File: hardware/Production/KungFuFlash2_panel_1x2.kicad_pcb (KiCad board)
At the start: 2 copper layers, 140.3 x 70 mm, 114 parts, among them J1 DNP, J2 USB_C_Receptacle_USB2.0, J3 DNP, Q1 BC817-40, SW1 ES411X-10XX-43X-16-B, SW2 ES411X-10XX-43X-16-B, SW3 ES411X-10XX-43X-16-B, U1 Edge Connector, Immersion gol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, U2 AMS1117-3.3, U3 STM32H7B0VBTx, Y1 25 MHz

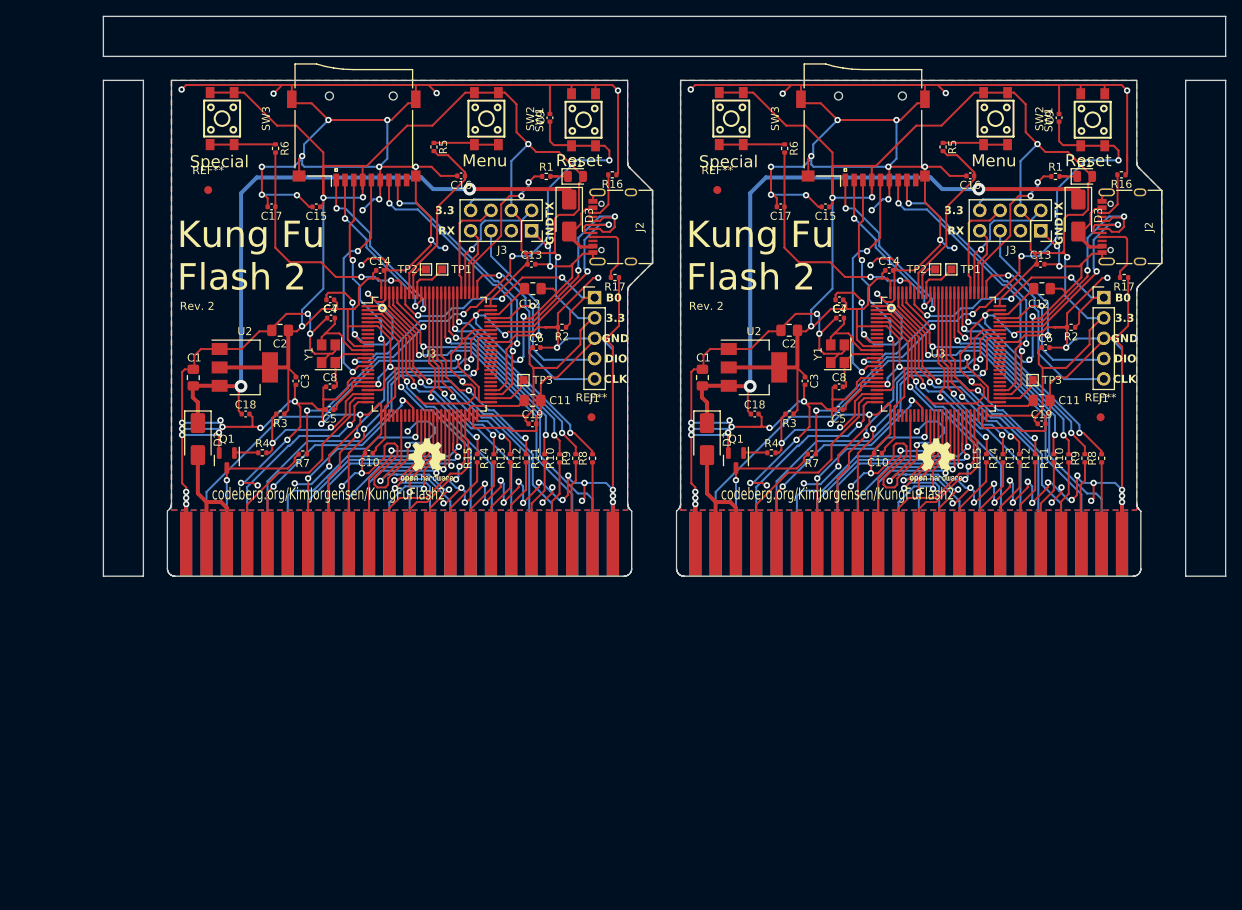
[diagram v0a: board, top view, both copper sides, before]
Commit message: Update PCB layout and add connector footprint
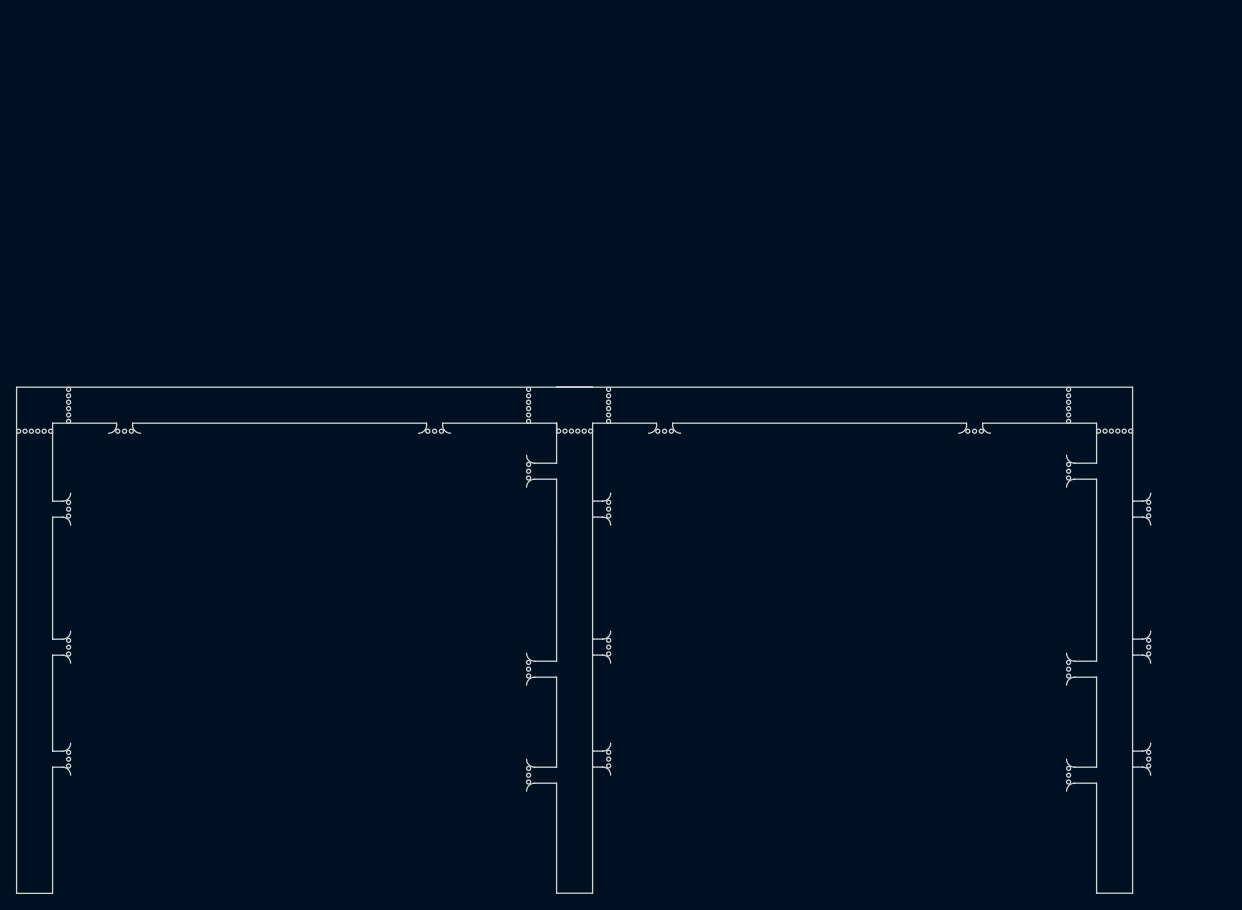
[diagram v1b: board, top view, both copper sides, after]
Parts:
- removed C1 (x2), C2 (x2): 10u, Capacitor_SMD:C_0805_2012Metric_Pad1.18x1.45mm_HandSolder
- removed C10 (x2), C13 (x2), C14 (x2), C15 (x2), C16 (x2), C17 (x2), C18 (x2), C19 (x2), C3 (x2), C4 (x2), C5 (x2), C6 (x2), C9 (x2): 100n, Capacitor_SMD:C_0402_1005Metric
- removed C11 (x2), C12 (x2): 2.2u, Capacitor_SMD:C_0805_2012Metric_Pad1.18x1.45mm_HandSolder
- removed C7 (x2), C8 (x2): 20p, Capacitor_SMD:C_0402_1005Metric
- removed D1 (x2): Green, LED_SMD:LED_0805_2012Metric
- removed D2 (x2), D3 (x2): D_Schottky, Diode_SMD:D_SMA
- removed J1 (x2): DNP, Connector_PinHeader_2.54mm:PinHeader_1x05_P2.54mm_Vertical
- removed J2 (x2): USB_C_Receptacle_USB2.0, Connector_USB:USB_C_Receptacle_XKB_U262-16XN-4BVC11
- removed J3 (x2): DNP, Connector_PinSocket_2.54mm:PinSocket_2x04_P2.54mm_Vertical
- removed Q1 (x2): BC817-40, Package_TO_SOT_SMD:SOT-23
- removed R1 (x2), R4 (x2), R5 (x2), R6 (x2), R7 (x2): 510R, Resistor_SMD:R_0402_1005Metric
- removed R10 (x2), R11 (x2), R12 (x2), R13 (x2), R14 (x2), R15 (x2), R8 (x2), R9 (x2): 100R, Resistor_SMD:R_0402_1005Metric
- removed R16 (x2), R17 (x2): 5.1k, Resistor_SMD:R_0402_1005Metric
- removed R2 (x2), R3 (x2): 10k, Resistor_SMD:R_0402_1005Metric
- removed the REF** at (91.5, 41.7)
- removed the REF** at (155.1, 41.7)
- removed the REF** at (182.4, 75.5)
- removed the REF** at (203.0, 70.1)
- removed the REF** at (118.8, 75.5)
- removed the REF** at (139.4, 70.1)
- removed SW1 (x2), SW2 (x2), SW3 (x2): ES411X-10XX-43X-16-B, easyECADDownloader:SW-SMD_4P-L4.5-W4.5-P3.00-LS6.7
- removed TP1 (x2), TP2 (x2), TP3 (x2): ~, TestPoint:TestPoint_Pad_1.0x1.0mm
- removed U1 (x2): Edge Connector, Immersion gold (1U"), Bevelling 45°, KungFuFlash2:C64-Cart
- removed U2 (x2): AMS1117-3.3, Package_TO_SOT_SMD:SOT-223-3_TabPin2
- removed U3 (x2): STM32H7B0VBTx, Package_QFP:LQFP-100_14x14mm_P0.5mm
- removed XS1 (x2): uSD_push_push, KungFuFlash2:Conn_uSDcard
- removed Y1 (x2): 25 MHz, Crystal:Crystal_SMD_3225-4Pin_3.2x2.5mm
- added REF**: BreakLine_1h_D0.5mm_P0.85mm, Panelization:BreakLine_1h_D0.5mm_P0.85mm, F.Cu at (69.4, 71.8)
- added REF**: MouseBite-Part_2.0x2.0mm_outset_D0.5mm_P0.85mm_3h, Panelization:MouseBite-Part_2.0x2.0mm_outset_D0.5mm_P0.85mm_3h, F.Cu at (119.8, 72.1)
- added REF**: BreakLine_1h_D0.5mm_P0.85mm, Panelization:BreakLine_1h_D0.5mm_P0.85mm, F.Cu at (141.5, 69.8)
- added REF**: BreakLine_1h_D0.5mm_P0.85mm, Panelization:BreakLine_1h_D0.5mm_P0.85mm, F.Cu at (74.0, 66.6)
- added REF**: BreakLine_1h_D0.5mm_P0.85mm, Panelization:BreakLine_1h_D0.5mm_P0.85mm, F.Cu at (199.0, 70.6)
- added REF**: BreakLine_1h_D0.5mm_P0.85mm, Panelization:BreakLine_1h_D0.5mm_P0.85mm, F.Cu at (205.2, 71.8)
- added REF**: BreakLine_1h_D0.5mm_P0.85mm, Panelization:BreakLine_1h_D0.5mm_P0.85mm, F.Cu at (74.0, 70.6)
- added REF**: BreakLine_1h_D0.5mm_P0.85mm, Panelization:BreakLine_1h_D0.5mm_P0.85mm, F.Cu at (135.3, 71.8)
- added REF**: MouseBite-Part_2.0x2.0mm_outset_D0.5mm_P0.85mm_3h, Panelization:MouseBite-Part_2.0x2.0mm_outset_D0.5mm_P0.85mm_3h, F.Cu at (148.5, 72.1)
- added REF**: BreakLine_1h_D0.5mm_P0.85mm, Panelization:BreakLine_1h_D0.5mm_P0.85mm, F.Cu at (141.5, 70.6)
- added REF**: MouseBite-Part_2.0x2.0mm_outset_D0.5mm_P0.85mm_3h, Panelization:MouseBite-Part_2.0x2.0mm_outset_D0.5mm_P0.85mm_3h, F.Cu at (74.3, 112.8)
- added REF**: BreakLine_1h_D0.5mm_P0.85mm, Panelization:BreakLine_1h_D0.5mm_P0.85mm, F.Cu at (131.5, 66.6)
- added REF**: BreakLine_1h_D0.5mm_P0.85mm, Panelization:BreakLine_1h_D0.5mm_P0.85mm, F.Cu at (138.5, 71.8)
- added REF**: MouseBite-Part_2.0x2.0mm_outset_D0.5mm_P0.85mm_3h, Panelization:MouseBite-Part_2.0x2.0mm_outset_D0.5mm_P0.85mm_3h, F.Cu at (198.8, 101.6)
- added REF**: BreakLine_1h_D0.5mm_P0.85mm, Panelization:BreakLine_1h_D0.5mm_P0.85mm, F.Cu at (206.8, 71.8)
- added REF**: BreakLine_1h_D0.5mm_P0.85mm, Panelization:BreakLine_1h_D0.5mm_P0.85mm, F.Cu at (199.0, 67.4)
- added REF**: BreakLine_1h_D0.5mm_P0.85mm, Panelization:BreakLine_1h_D0.5mm_P0.85mm, F.Cu at (74.0, 67.4)
- added REF**: BreakLine_1h_D0.5mm_P0.85mm, Panelization:BreakLine_1h_D0.5mm_P0.85mm, F.Cu at (131.5, 69.0)
- added REF**: BreakLine_1h_D0.5mm_P0.85mm, Panelization:BreakLine_1h_D0.5mm_P0.85mm, F.Cu at (202.8, 71.8)
- added REF**: MouseBite-Part_2.0x2.0mm_outset_D0.5mm_P0.85mm_3h, Panelization:MouseBite-Part_2.0x2.0mm_outset_D0.5mm_P0.85mm_3h, F.Cu at (141.8, 81.6)
- added REF**: BreakLine_1h_D0.5mm_P0.85mm, Panelization:BreakLine_1h_D0.5mm_P0.85mm, F.Cu at (71.8, 71.8)
- added REF**: MouseBite-Part_2.0x2.0mm_outset_D0.5mm_P0.85mm_3h, Panelization:MouseBite-Part_2.0x2.0mm_outset_D0.5mm_P0.85mm_3h, F.Cu at (131.3, 76.8)
- added REF**: BreakLine_1h_D0.5mm_P0.85mm, Panelization:BreakLine_1h_D0.5mm_P0.85mm, F.Cu at (141.5, 69.0)
- added REF**: BreakLine_1h_D0.5mm_P0.85mm, Panelization:BreakLine_1h_D0.5mm_P0.85mm, F.Cu at (74.0, 68.2)
- added REF**: BreakLine_1h_D0.5mm_P0.85mm, Panelization:BreakLine_1h_D0.5mm_P0.85mm, F.Cu at (68.6, 71.8)
- added REF**: MouseBite-Part_2.0x2.0mm_outset_D0.5mm_P0.85mm_3h, Panelization:MouseBite-Part_2.0x2.0mm_outset_D0.5mm_P0.85mm_3h, F.Cu at (209.3, 98.8)
- added REF**: BreakLine_1h_D0.5mm_P0.85mm, Panelization:BreakLine_1h_D0.5mm_P0.85mm, F.Cu at (70.2, 71.8)
- added REF**: BreakLine_1h_D0.5mm_P0.85mm, Panelization:BreakLine_1h_D0.5mm_P0.85mm, F.Cu at (203.6, 71.8)
- added REF**: BreakLine_1h_D0.5mm_P0.85mm, Panelization:BreakLine_1h_D0.5mm_P0.85mm, F.Cu at (131.5, 68.2)
- added REF**: MouseBite-Part_2.0x2.0mm_outset_D0.5mm_P0.85mm_3h, Panelization:MouseBite-Part_2.0x2.0mm_outset_D0.5mm_P0.85mm_3h, F.Cu at (198.8, 114.8)
- added REF**: BreakLine_1h_D0.5mm_P0.85mm, Panelization:BreakLine_1h_D0.5mm_P0.85mm, F.Cu at (137.7, 71.8)
- added REF**: MouseBite-Part_2.0x2.0mm_outset_D0.5mm_P0.85mm_3h, Panelization:MouseBite-Part_2.0x2.0mm_outset_D0.5mm_P0.85mm_3h, F.Cu at (74.3, 98.8)
- added REF**: BreakLine_1h_D0.5mm_P0.85mm, Panelization:BreakLine_1h_D0.5mm_P0.85mm, F.Cu at (67.8, 71.8)
- added REF**: BreakLine_1h_D0.5mm_P0.85mm, Panelization:BreakLine_1h_D0.5mm_P0.85mm, F.Cu at (74.0, 69.0)
- added REF**: MouseBite-Part_2.0x2.0mm_outset_D0.5mm_P0.85mm_3h, Panelization:MouseBite-Part_2.0x2.0mm_outset_D0.5mm_P0.85mm_3h, F.Cu at (141.8, 98.8)
- added REF**: BreakLine_1h_D0.5mm_P0.85mm, Panelization:BreakLine_1h_D0.5mm_P0.85mm, F.Cu at (199.0, 69.8)
- added REF**: MouseBite-Part_2.0x2.0mm_outset_D0.5mm_P0.85mm_3h, Panelization:MouseBite-Part_2.0x2.0mm_outset_D0.5mm_P0.85mm_3h, F.Cu at (74.3, 81.6)
- added REF**: MouseBite-Part_2.0x2.0mm_outset_D0.5mm_P0.85mm_3h, Panelization:MouseBite-Part_2.0x2.0mm_outset_D0.5mm_P0.85mm_3h, F.Cu at (209.3, 112.8)
- added REF**: BreakLine_1h_D0.5mm_P0.85mm, Panelization:BreakLine_1h_D0.5mm_P0.85mm, F.Cu at (199.0, 66.6)
- added REF**: MouseBite-Part_2.0x2.0mm_outset_D0.5mm_P0.85mm_3h, Panelization:MouseBite-Part_2.0x2.0mm_outset_D0.5mm_P0.85mm_3h, F.Cu at (131.3, 114.8)
- added REF**: BreakLine_1h_D0.5mm_P0.85mm, Panelization:BreakLine_1h_D0.5mm_P0.85mm, F.Cu at (136.1, 71.8)
- added REF**: BreakLine_1h_D0.5mm_P0.85mm, Panelization:BreakLine_1h_D0.5mm_P0.85mm, F.Cu at (141.5, 66.6)
- added REF**: BreakLine_1h_D0.5mm_P0.85mm, Panelization:BreakLine_1h_D0.5mm_P0.85mm, F.Cu at (74.0, 69.8)
- added REF**: BreakLine_1h_D0.5mm_P0.85mm, Panelization:BreakLine_1h_D0.5mm_P0.85mm, F.Cu at (139.3, 71.8)
- added REF**: MouseBite-Part_2.0x2.0mm_outset_D0.5mm_P0.85mm_3h, Panelization:MouseBite-Part_2.0x2.0mm_outset_D0.5mm_P0.85mm_3h, F.Cu at (187.3, 72.1)
- added REF**: BreakLine_1h_D0.5mm_P0.85mm, Panelization:BreakLine_1h_D0.5mm_P0.85mm, F.Cu at (131.5, 67.4)
- added REF**: MouseBite-Part_2.0x2.0mm_outset_D0.5mm_P0.85mm_3h, Panelization:MouseBite-Part_2.0x2.0mm_outset_D0.5mm_P0.85mm_3h, F.Cu at (131.3, 101.6)
- added REF**: BreakLine_1h_D0.5mm_P0.85mm, Panelization:BreakLine_1h_D0.5mm_P0.85mm, F.Cu at (131.5, 70.6)
- added REF**: BreakLine_1h_D0.5mm_P0.85mm, Panelization:BreakLine_1h_D0.5mm_P0.85mm, F.Cu at (204.4, 71.8)
- added REF**: BreakLine_1h_D0.5mm_P0.85mm, Panelization:BreakLine_1h_D0.5mm_P0.85mm, F.Cu at (131.5, 69.8)
- added REF**: MouseBite-Part_2.0x2.0mm_outset_D0.5mm_P0.85mm_3h, Panelization:MouseBite-Part_2.0x2.0mm_outset_D0.5mm_P0.85mm_3h, F.Cu at (198.8, 76.8)
- added REF**: BreakLine_1h_D0.5mm_P0.85mm, Panelization:BreakLine_1h_D0.5mm_P0.85mm, F.Cu at (71.0, 71.8)
- added REF**: BreakLine_1h_D0.5mm_P0.85mm, Panelization:BreakLine_1h_D0.5mm_P0.85mm, F.Cu at (136.9, 71.8)
- added REF**: MouseBite-Part_2.0x2.0mm_outset_D0.5mm_P0.85mm_3h, Panelization:MouseBite-Part_2.0x2.0mm_outset_D0.5mm_P0.85mm_3h, F.Cu at (209.3, 81.6)
- added REF**: MouseBite-Part_2.0x2.0mm_outset_D0.5mm_P0.85mm_3h, Panelization:MouseBite-Part_2.0x2.0mm_outset_D0.5mm_P0.85mm_3h, F.Cu at (141.8, 112.8)
- added REF**: BreakLine_1h_D0.5mm_P0.85mm, Panelization:BreakLine_1h_D0.5mm_P0.85mm, F.Cu at (141.5, 67.4)
- added REF**: BreakLine_1h_D0.5mm_P0.85mm, Panelization:BreakLine_1h_D0.5mm_P0.85mm, F.Cu at (199.0, 69.0)
- added REF**: BreakLine_1h_D0.5mm_P0.85mm, Panelization:BreakLine_1h_D0.5mm_P0.85mm, F.Cu at (199.0, 68.2)
- added REF**: MouseBite-Part_2.0x2.0mm_outset_D0.5mm_P0.85mm_3h, Panelization:MouseBite-Part_2.0x2.0mm_outset_D0.5mm_P0.85mm_3h, F.Cu at (81.0, 72.1)
- added REF**: BreakLine_1h_D0.5mm_P0.85mm, Panelization:BreakLine_1h_D0.5mm_P0.85mm, F.Cu at (141.5, 68.2)
- added REF**: BreakLine_1h_D0.5mm_P0.85mm, Panelization:BreakLine_1h_D0.5mm_P0.85mm, F.Cu at (206.0, 71.8)
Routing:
- net Board_1-GND: track 640.0 -> 0.00 mm, vias 72 -> 0
- net Board_0-GND: track 640.0 -> 0.00 mm, vias 72 -> 0
- net Board_1-+3V3: track 266.7 -> 0.00 mm, vias 7 -> 0
- net Board_0-+3V3: track 266.7 -> 0.00 mm, vias 7 -> 0
- net Board_1-Net-(D2-K): track 81.0 -> 0.00 mm, vias 2 -> 0
- net Board_0-Net-(D2-K): track 81.0 -> 0.00 mm, vias 2 -> 0
- net Board_1-/~{RST}: track 60.3 -> 0.00 mm, vias 4 -> 0
- net Board_0-/~{RST}: track 60.3 -> 0.00 mm, vias 4 -> 0
- net Board_1-/~{ROMH}: track 52.9 -> 0.00 mm, vias 1 -> 0
- net Board_0-/~{ROMH}: track 52.9 -> 0.00 mm, vias 1 -> 0
- net Board_1-/PHI2: track 47.1 -> 0.00 mm, vias 1 -> 0
- net Board_0-/PHI2: track 47.1 -> 0.00 mm, vias 1 -> 0
- net Board_1-/A0: track 45.9 -> 0.00 mm, vias 1 -> 0
- net Board_0-/A0: track 45.9 -> 0.00 mm, vias 1 -> 0
- net Board_1-/A1: track 45.4 -> 0.00 mm, vias 1 -> 0
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- removed copper zone on B.Cu, net Board_0-GND
- removed copper zone on F.Cu, net Board_0-GND
- removed copper zone on B.Cu, net Board_1-GND
- removed copper zone on F.Cu, net Board_1-GND
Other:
- board size 140.3 x 70 mm -> 140.8 x 63.3 mm
- board text removed: "3.3"
- board text removed: "B0"
- board text removed: "CLK"
- board text removed: "DIO"
- board text removed: "GND"
- board text removed: "Kung Fu Flash 2"
- board text removed: "Menu"
- board text removed: "RX"
- board text removed: "Reset"
- board text removed: "Rev. 2"
- board text removed: "Special"
- board text removed: "TX"
- board text removed: "codeberg.org/KimJorgensen/KungFuFlash2"
